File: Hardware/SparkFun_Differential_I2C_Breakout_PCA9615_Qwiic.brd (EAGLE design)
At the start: 49.5 x 25.4 mm, 40 parts, among them J3 RJ45, U1 PCA9615

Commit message: Pushing design before Redboard Review
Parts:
- removed JP6: (no value), SparkX:1X04
- removed LOGO2: SFE_LOGO_NAME.1_INCH, SparkFun-Aesthetics:SFE_LOGO_NAME_.1
- removed R1A, R2A, R3A, R4A, R5A, R6A: DNP, SparkFun-Resistors:AXIAL-0.3
- added J5: (no value), SparkFun-Connectors:1X01
- added J6: (no value), SparkX:1X04
- added LOGO3: SFE_LOGO_NAME.1_INCH, SparkFun-Aesthetics:SFE_LOGO_NAME_.1
- R1, R3, R4, R6: value 750 -> 390
- R2, R5: value 750 -> 100
- moved J4 29.0 mm to (29.2, 24.1), turned to 180 degrees
- moved LOGO1 27.4 mm to (19.1, 7.37), turned to 0 degrees
- moved FD1 22.9 mm to (5.08, 1.27)
- moved FD3 22.9 mm to (5.08, 1.27)
- moved FD2 21.4 mm to (43.8, 24.8)
- moved FD4 21.4 mm to (43.8, 24.8)
- moved C3 7.62 mm to (15.9, 17.1), turned to 180 degrees
- moved C2 6.48 mm to (22.2, 17.1), turned to 0 degrees
- moved C1 6.02 mm to (15.9, 15.2), turned to 180 degrees
- moved JP3 5.71 mm to (28.6, 12.1)
- moved JP1 5.46 mm to (19.1, 17.1), turned to 0 degrees
- moved R7 5.08 mm to (10.2, 10.2)
- moved R8 5.08 mm to (10.2, 15.2)
- moved C4 4.49 mm to (22.2, 15.2), turned to 0 degrees
- moved J3 4.45 mm to (41.3, 12.7)
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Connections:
- net DSCL+: no longer R1A.P$1, R2A.P$2
- net DSCL-: no longer R2A.P$1, R3A.P$2
- net DSDA+: no longer R4A.P$1, R5A.P$2
- net DSDA-: no longer R5A.P$1, R6A.P$2
- net EN: now also J5.1; no longer J4.1
- net GND: now also J4.1, J6.1; no longer JP6.1, R3A.P$1, R6A.P$1
- net SCL: now also J6.4; no longer JP6.4
- net SDA: now also J6.3; no longer JP6.3
- net VDD_A: now also J6.2; no longer JP6.2
- net VDD_B: no longer R1A.P$2, R4A.P$2
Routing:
- net VDD_B: track 79.2 -> 35.1 mm, vias 4 -> 2
- net DSCL-: track 35.2 -> 17.6 mm
- net DSCL+: track 35.4 -> 19.0 mm
- net SDA: track 52.8 -> 40.1 mm, vias 1 -> 2
- net DSDA-: track 32.5 -> 21.6 mm
- net DSDA+: track 30.1 -> 21.4 mm
- net EN: track 24.6 -> 20.2 mm
- net GND: track 3.84 -> 0.28 mm, vias 14 -> 3
- net SCL: track 42.7 -> 45.0 mm
- net N$1: track 2.03 -> 3.30 mm
- net N$2: track 2.03 -> 3.30 mm
- net N$3: track 2.32 -> 3.26 mm
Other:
- board size 49.5 x 25.4 mm -> 44.5 x 25.4 mm
- board text added: "Differential I2C PCA9615-Qwiic"
- board text added: "V10"
- board text removed: "1"
- board text removed: "2"
- board text removed: "3"
- board text removed: "4"
- board text removed: "5"
- board text removed: "6"
- board text removed: "DSCL"
- board text removed: "DSDA"
- board text removed: "PCA9615"
- board text removed: "Qwiic Long-Distance"
- board text removed: "V01"

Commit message: Adding PCA9615 to SFE Eagle Library
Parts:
- U1: device Openponics:TSSOP10 -> SparkFun-IC-Comms:TSSOP10
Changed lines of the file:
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@@
 <setting verticaltext="up"/>
 </settings>
-<grid distance="0.025" unitdist="inch" unit="inch" style="lines" multiple="1" display="yes" altdistance="0.005" altunitdist="inch" altunit="inch"/>
+<grid distance="0.05" unitdist="inch" unit="inch" style="lines" multiple="1" display="yes" altdistance="0.005" altunitdist="inch" altunit="inch"/>
 <layers>
 <layer number="1" name="Top" color="4" fill="1" visible="yes" active="yes"/>
@@
 <layer number="47" name="Measures" color="7" fill="1" visible="no" active="yes"/>
 <layer number="48" name="Document" color="7" fill="1" visible="no" active="yes"/>
-<layer number="49" name="Reference" color="7" fill="1" visible="yes" active="yes"/>
+<layer number="49" name="Reference" color="7" fill="1" visible="no" active="yes"/>
 <layer number="50" name="dxf" color="7" fill="1" visible="no" active="no"/>
 <layer number="51" name="tDocu" color="6" fill="1" visible="yes" active="yes"/>
@@
 <attribute name="PROD_ID" value="CONN-13694" x="12.7" y="5.08" size="1.778" layer="27" font="vector" ratio="15" display="off"/>
 </element>
-<element name="U1" library="Openponics" package="TSSOP10" value="PCA9615" x="19.05" y="12.7"/>
+<element name="U1" library="SparkFun-IC-Comms" package="TSSOP10" value="PCA9615" x="19.05" y="12.7">
+<attribute name="PROD_ID" value="PENDING" x="19.05" y="12.7" size="1.778" layer="27" display="off"/>
+</element>
 <element name="J2" library="SparkFun-Connectors" package="1X04_1MM_RA" value="" x="12.7" y="20.32" rot="R180">
 <attribute name="PROD_ID" value="CONN-13694" x="21.59" y="10.16" size="1.778" layer="27" font="vector" ratio="15" rot="R180" display="off"/>

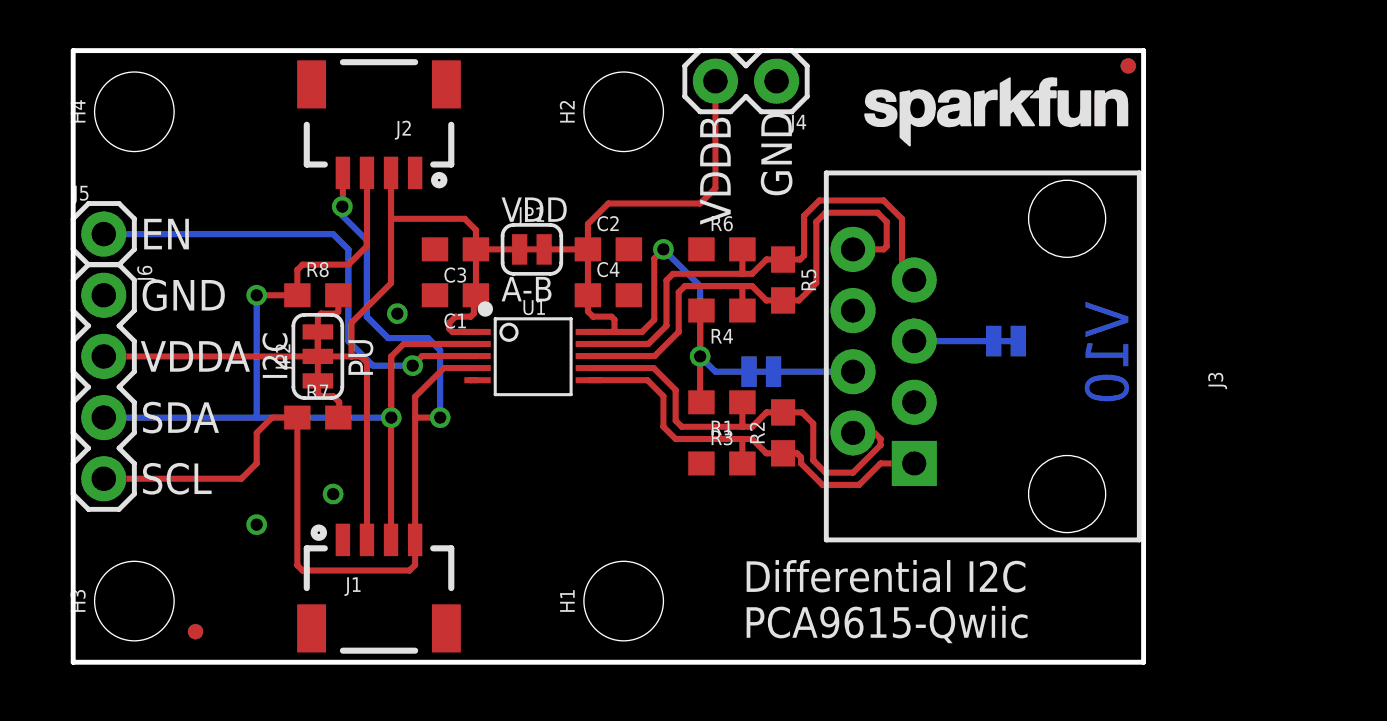
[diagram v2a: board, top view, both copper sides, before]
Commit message: ENG Design Checklist changes
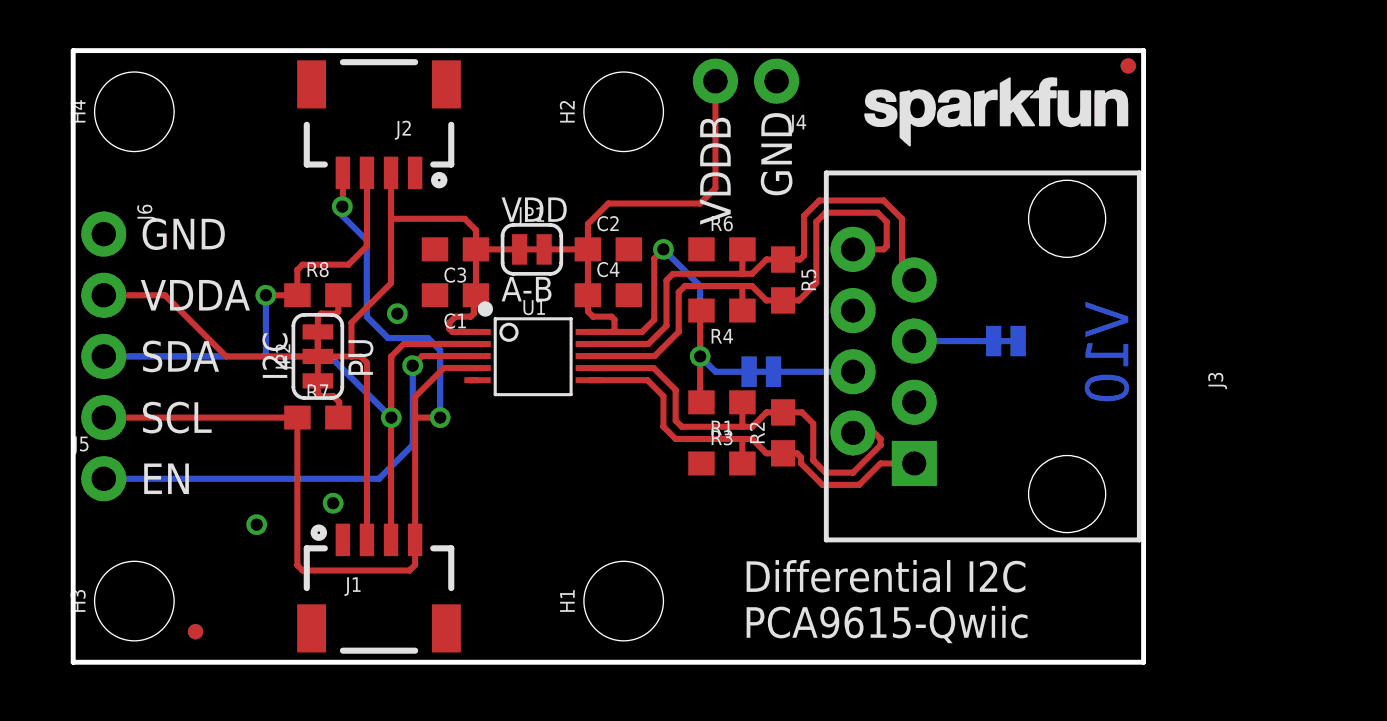
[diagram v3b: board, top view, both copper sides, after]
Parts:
- J4: device SparkFun-Connectors:1X02 -> SparkFun-Connectors:1X02_NO_SILK
- J5: device SparkFun-Connectors:1X01 -> SparkFun-Connectors:1X01_NO_SILK
- J6: device SparkX:1X04 -> SparkX:1X04_NO_SILK
- moved J5 10.2 mm to (1.27, 7.62)
- moved J6 2.54 mm to (1.27, 17.8)
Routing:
- net SDA: track 40.1 -> 38.2 mm
- net SCL: track 45.0 -> 43.2 mm
- net VDD_A: track 38.7 -> 39.8 mm
- net EN: track 20.2 -> 19.6 mm
